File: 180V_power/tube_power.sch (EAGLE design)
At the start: 22 parts, among them IC1 NE555D, Q1 IRF740S, U1 TLV1117-5SOT-223, U2 2N7002

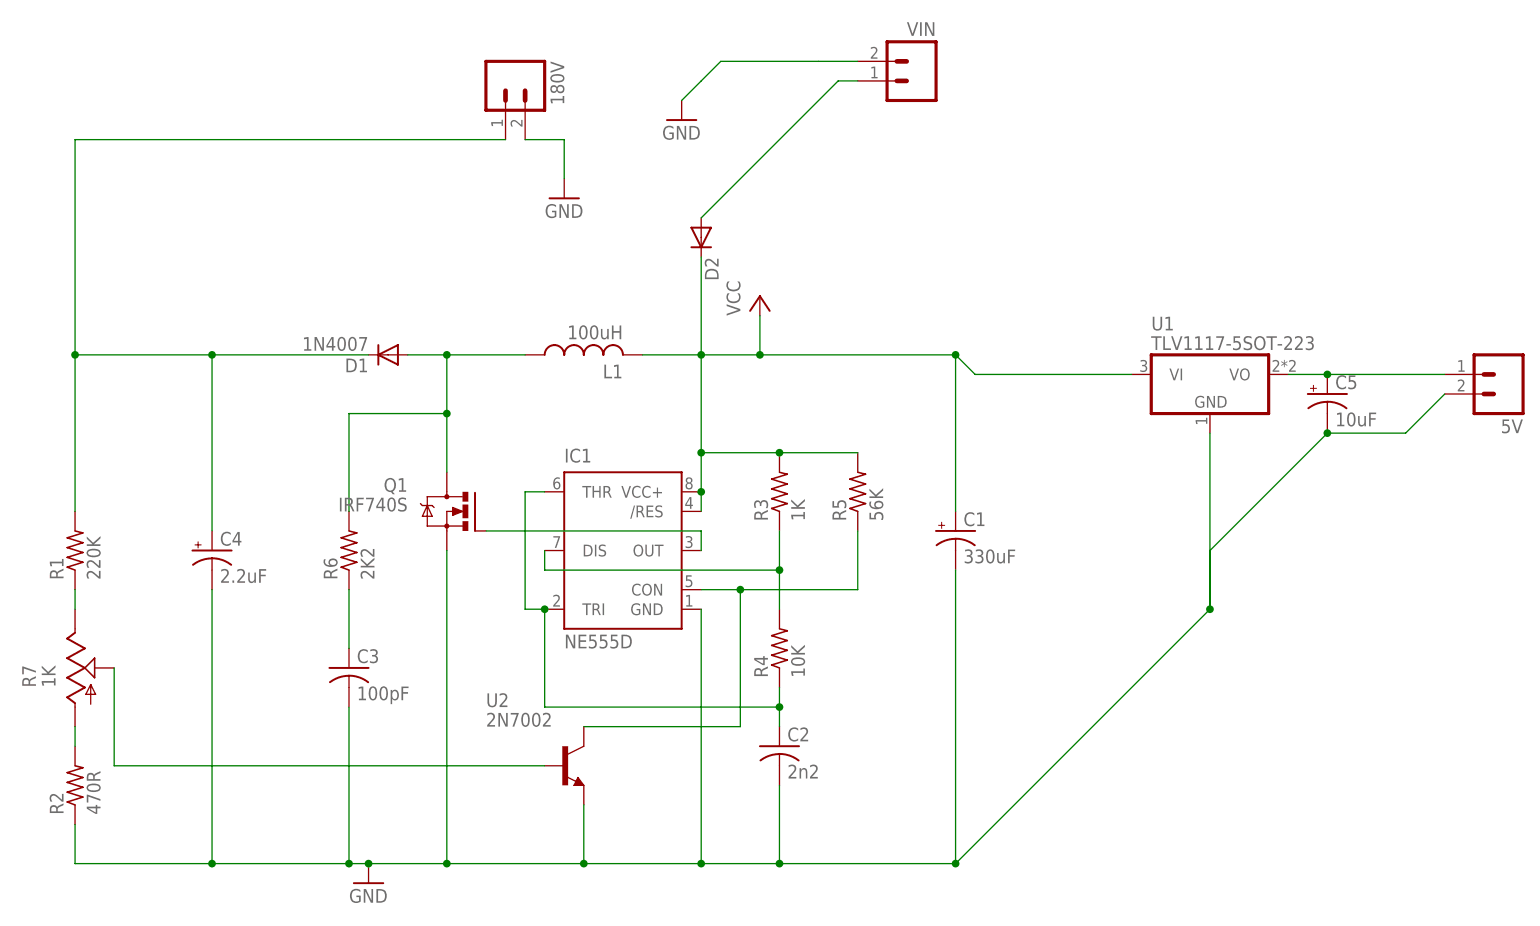
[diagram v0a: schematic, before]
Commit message: new 180V board design
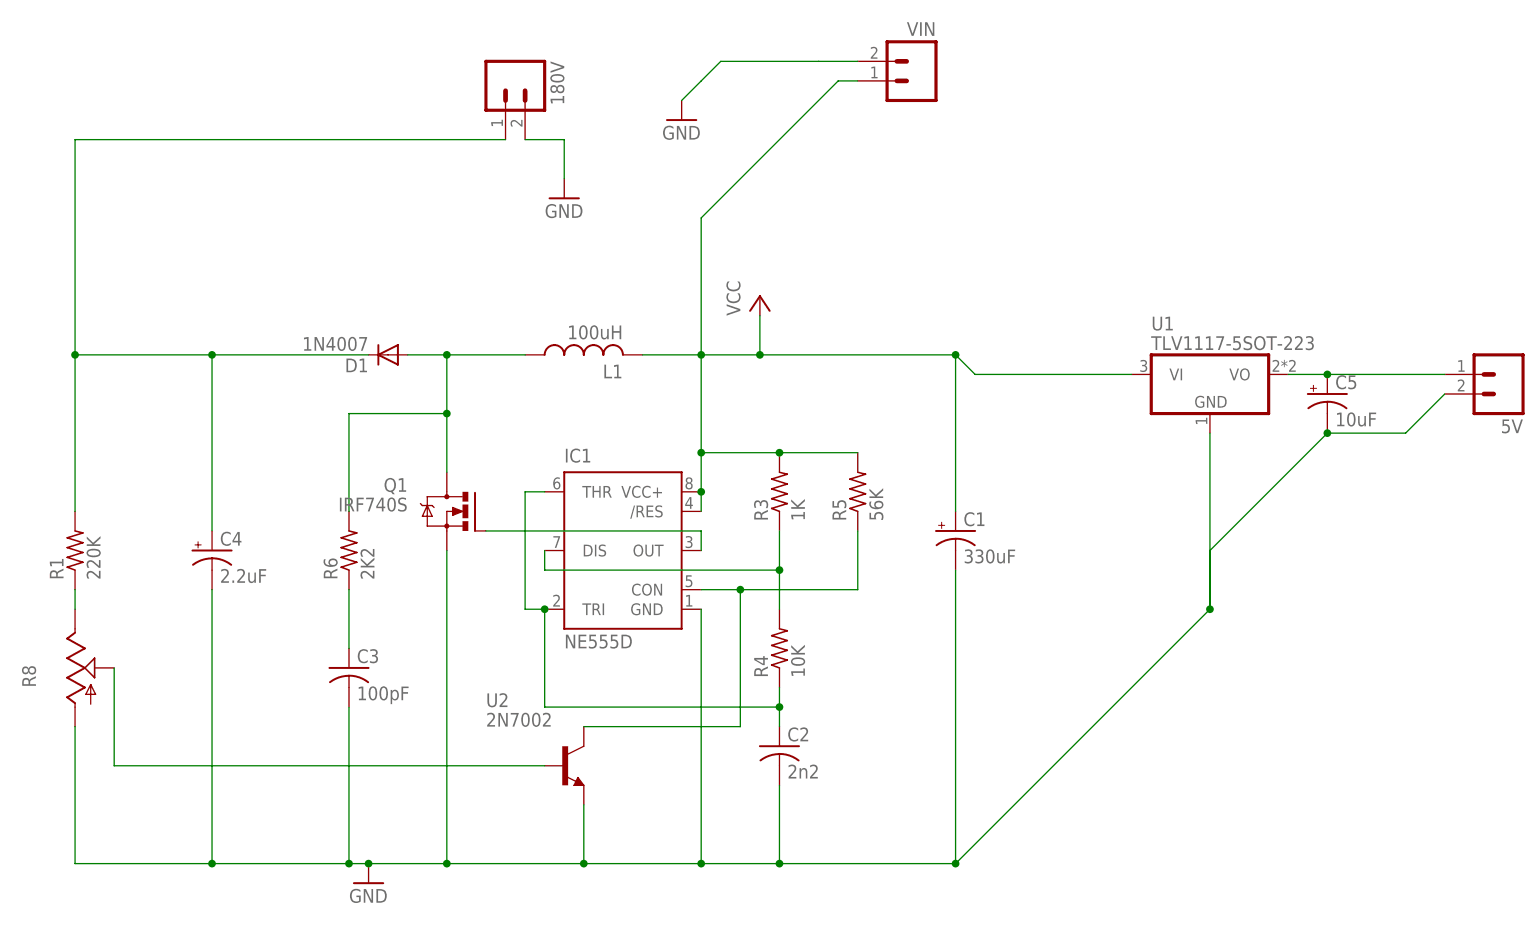
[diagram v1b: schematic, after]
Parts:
- removed D2: (no value), iStivi - RCLD:DIODESMA
- removed R2: 470R, iStivi - RCLD:RESISTOR0207/10
- removed R7: 1K, iStivi - RCLD:TRIM_POTCA6V
- added R8: (no value), iStivi - RCLD:TRIM_POTEVM2N
- C4: device iStivi - RCLD:CAPACITOR_POLE5-10.5 -> iStivi - RCLD:CAPACITOR_POLE3.5-8
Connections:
- removed net R2: R2.2, R7.A
- removed net VAR: R7.S, U2.B
- net GND: now also R8.A; no longer R2.1
- net N$1: now also R8.S, U2.B; no longer D2.A, VIN.1
- net R1: now also R8.E; no longer R7.E
- net VCC: now also VIN.1; no longer D2.C

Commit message: added diode and resistor to 180V power
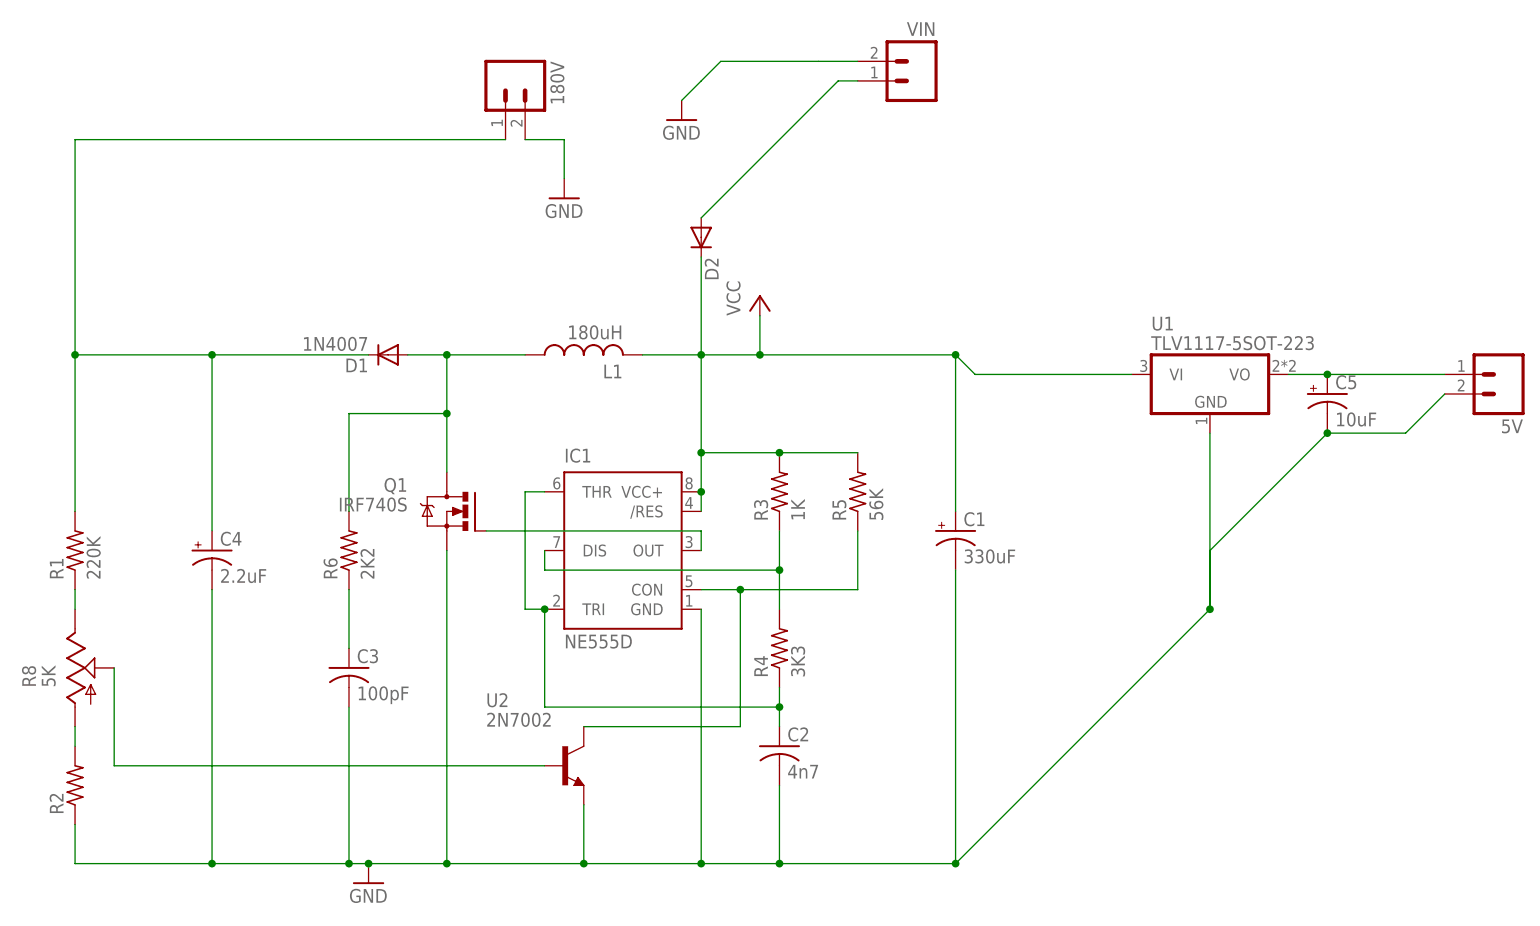
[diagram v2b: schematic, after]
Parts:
- added D2: (no value), iStivi - RCLD:DIODESOD-80
- added R2: (no value), iStivi - RCLD:RESISTORR1206
- C2: value 2n2 -> 4n7
- L1: value 100uH -> 180uH
- R4: value 10K -> 3K3
- R8: value (none) -> 5K
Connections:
- new net N$2: D2.A, VIN.1
- new net N$3: R2.2, R8.A
- net GND: now also R2.1; no longer R8.A
- net VCC: now also D2.C; no longer VIN.1
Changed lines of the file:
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@@
 <layer number="25" name="tNames" color="7" fill="1" visible="yes" active="no"/>
 <layer number="26" name="bNames" color="7" fill="1" visible="yes" active="no"/>
-<layer number="27" name="tValues" color="1" fill="1" visible="yes" active="no"/>
+<layer number="27" name="tValues" color="6" fill="1" visible="yes" active="no"/>
 <layer number="28" name="bValues" color="5" fill="1" visible="yes" active="no"/>
 <layer number="29" name="tStop" color="7" fill="3" visible="no" active="no"/>
@@
 <layer number="97" name="Info" color="7" fill="1" visible="yes" active="yes"/>
 <layer number="98" name="Guide" color="6" fill="1" visible="yes" active="yes"/>
+<layer number="99" name="SpiceOrder" color="5" fill="1" visible="yes" active="yes"/>
 <layer number="100" name="Muster" color="7" fill="1" visible="no" active="no"/>
 <layer number="101" name="Patch_Top" color="12" fill="4" visible="yes" active="yes"/>
@@
 <part name="C1" library="iStivi - RCLD" deviceset="CAPACITOR_POL" device="E5-10.5" value="330uF"/>
 <part name="R5" library="iStivi - RCLD" deviceset="RESISTOR" device="R0805" value="56K"/>
-<part name="R4" library="iStivi - RCLD" deviceset="RESISTOR" device="R0805" value="10K"/>
+<part name="R4" library="iStivi - RCLD" deviceset="RESISTOR" device="R0805" value="3K3"/>
 <part name="R3" library="iStivi - RCLD" deviceset="RESISTOR" device="R0805" value="1K"/>
 <part name="R1" library="iStivi - RCLD" deviceset="RESISTOR" device="0207/10" value="220K"/>
 <part name="R6" library="iStivi - RCLD" deviceset="RESISTOR" device="R0805" value="2K2"/>
 <part name="C3" library="iStivi - RCLD" deviceset="CAPACITOR" device="C0805K" value="100pF"/>
-<part name="C2" library="iStivi - RCLD" deviceset="CAPACITOR" device="C0805K" value="2n2"/>
+<part name="C2" library="iStivi - RCLD" deviceset="CAPACITOR" device="C0805K" value="4n7"/>
 <part name="GND1" library="iStivi - Supply" deviceset="GND" device=""/>
 <part name="180V" library="iStivi - Header-Connector" deviceset="M02" device="3.5MM"/>
@@
 <part name="U1" library="iStivi - Transistor-FET-reg" deviceset="TLV1117-5" device="SOT-223"/>
 <part name="U2" library="iStivi - Transistor-FET-reg" deviceset="BC817" device="" value="2N7002"/>
-<part name="L1" library="iStivi - RCLD" deviceset="INDUCTOR" device="" value="100uH"/>
+<part name="L1" library="iStivi - RCLD" deviceset="INDUCTOR" device="" value="180uH"/>
 <part name="Q1" library="iStivi - Transistor-FET-reg" deviceset="IRF740" device="S"/>
 <part name="P+1" library="iStivi - Supply" deviceset="VCC" device=""/>
-<part name="R8" library="iStivi - RCLD" deviceset="TRIM_POT" device="EVM2N"/>
+<part name="R8" library="iStivi - RCLD" deviceset="TRIM_POT" device="EVM2N" value="5K"/>
+<part name="D2" library="iStivi - RCLD" deviceset="DIODE" device="SOD-80"/>
+<part name="R2" library="iStivi - RCLD" deviceset="RESISTOR" device="R1206"/>
 </parts>
 <sheets>
@@
 <instance part="P+1" gate="VCC" x="88.9" y="66.04"/>
 <instance part="R8" gate="G$1" x="0" y="17.78"/>
+<instance part="D2" gate="G$1" x="81.28" y="73.66" rot="R270"/>
+<instance part="R2" gate="G$1" x="0" y="2.54" rot="R90"/>
 </instances>
 <busses>
@@
 <pinref part="U2" gate="G$1" pin="E"/>
 <pinref part="Q1" gate="G$1" pin="S"/>
-<pinref part="R8" gate="G$1" pin="A"/>
-<wire x1="0" y1="10.16" x2="0" y2="-7.62" width="0.1524" layer="91"/>
+<pinref part="R2" gate="G$1" pin="1"/>
+<wire x1="0" y1="-2.54" x2="0" y2="-7.62" width="0.1524" layer="91"/>
 </segment>
 <segment>
@@
 <wire x1="88.9" y1="63.5" x2="88.9" y2="58.42" width="0.1524" layer="91"/>
 <junction x="88.9" y="58.42"/>
-<wire x1="81.28" y1="58.42" x2="81.28" y2="76.2" width="0.1524" layer="91"/>
-<pinref part="VIN" gate="G$1" pin="1"/>
-<wire x1="101.6" y1="93.98" x2="99.06" y2="93.98" width="0.1524" layer="91"/>
-<wire x1="81.28" y1="76.2" x2="99.06" y2="93.98" width="0.1524" layer="91"/>
+<pinref part="D2" gate="G$1" pin="C"/>
+<wire x1="81.28" y1="58.42" x2="81.28" y2="71.12" width="0.1524" layer="91"/>
 </segment>
 </net>
@@
 </segment>
 </net>
+<net name="N$2" class="0">
+<segment>
+<pinref part="VIN" gate="G$1" pin="1"/>
+<wire x1="101.6" y1="93.98" x2="99.06" y2="93.98" width="0.1524" layer="91"/>
+<pinref part="D2" gate="G$1" pin="A"/>
+<wire x1="81.28" y1="76.2" x2="99.06" y2="93.98" width="0.1524" layer="91"/>
+</segment>
+</net>
+<net name="N$3" class="0">
+<segment>
+<pinref part="R2" gate="G$1" pin="2"/>
+<pinref part="R8" gate="G$1" pin="A"/>
+<wire x1="0" y1="7.62" x2="0" y2="10.16" width="0.1524" layer="91"/>
+</segment>
+</net>
